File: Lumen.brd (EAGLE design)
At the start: 59.6 x 24 mm, 32 parts, among them J1 AVR_SPI_PRG_6PTH, U1 Tiny45-20-SMT, Y1 8MHZ

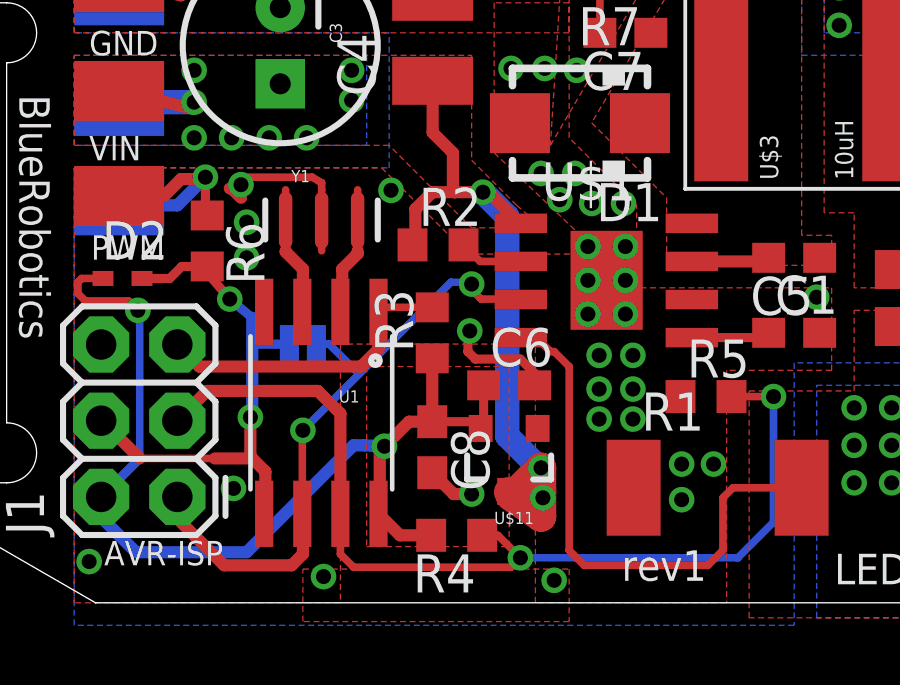
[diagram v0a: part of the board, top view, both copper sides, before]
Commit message: Fixed two minor issues in the layout with ground per J.N. suggestion. Ordering a prototype tomorrow.
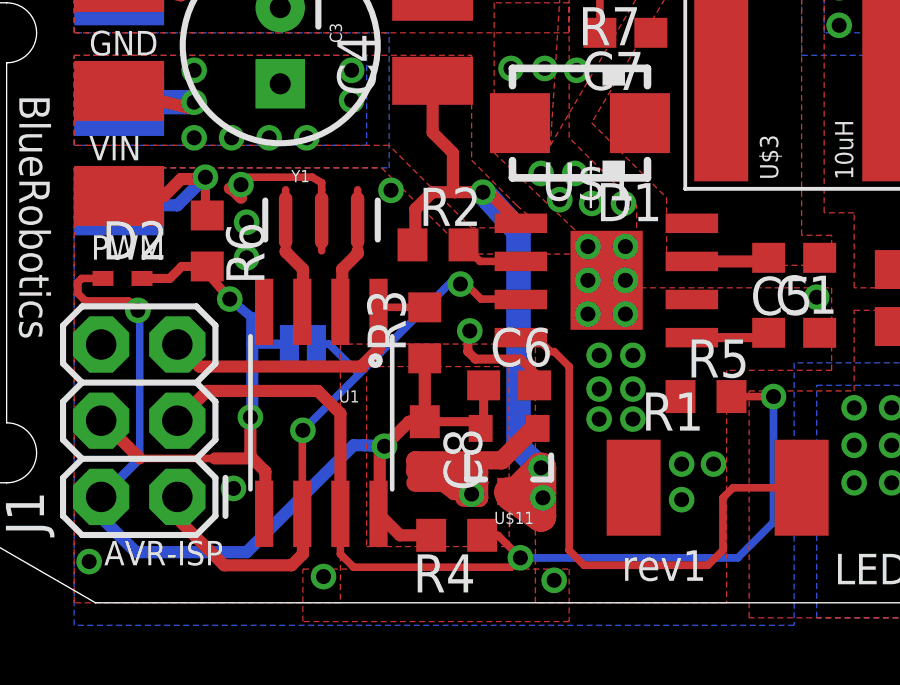
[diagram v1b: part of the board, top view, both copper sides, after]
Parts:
- moved C8 0.25 mm to (13.9, 5.19)
- moved R3 0.25 mm to (13.9, 9.00)
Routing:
- net GND: track 15.1 -> 25.9 mm
- net LED-PWM: track 21.7 -> 22.3 mm
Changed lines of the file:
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@@
 <element name="R1" library="resistor" package="R2512" value="0.082 1W" x="23.7" y="3.835"/>
 <element name="R2" library="resistor" package="R0603" value="140K" x="14.38" y="11.93"/>
-<element name="R3" library="resistor" package="R0603" value="10K" x="14.1875" y="9" rot="R90"/>
+<element name="R3" library="resistor" package="R0603" value="10K" x="13.9375" y="9" rot="R90"/>
 <element name="R4" library="resistor" package="R0603" value="3.3K 1%" x="15" y="2.25" rot="R180"/>
 <element name="R5" library="resistor" package="R0603" value="10K NTC" x="23.3125" y="6.875"/>
@@
 <attribute name="PROD_ID" value="IC-08922" x="10.49" y="6.32" size="1.778" layer="27" rot="R180" display="off"/>
 </element>
-<element name="C8" library="resistor" package="C0603" value="0.1uF" x="14.1875" y="5.1875" rot="R270"/>
+<element name="C8" library="resistor" package="C0603" value="0.1uF" x="13.9375" y="5.1875" rot="R270"/>
 <element name="Y1" library="SparkFun-FreqCtrl" package="RESONATOR-SMD" value="8MHZ" x="10.5" y="12.75">
 <attribute name="PROD_ID" value="XTAL-08900" x="10.5" y="12.75" size="1.778" layer="27" display="off"/>
@@
 <via x="18.4375" y="13.4375" extent="1-16" drill="0.5"/>
 <wire x1="15.5" y1="3.625" x2="14.9" y2="3.625" width="0.4064" layer="1"/>
-<wire x1="14.9" y1="3.625" x2="14.1875" y2="4.3375" width="0.4064" layer="1"/>
+<wire x1="14.9" y1="3.625" x2="13.9375" y2="4.3375" width="0.4064" layer="1"/>
 <polygon width="0.4064" layer="1" isolate="0.254" thermals="no">
 <vertex x="2.25" y="14.5"/>
@@
 <via x="19.75" y="7.125" extent="1-16" drill="0.5"/>
 <via x="19.75" y="6.125" extent="1-16" drill="0.5"/>
+<wire x1="17.75" y1="5.875" x2="17.625" y2="5.875" width="0.6096" layer="1"/>
+<wire x1="17.625" y1="5.875" x2="16.5" y2="4.75" width="0.6096" layer="1"/>
+<wire x1="16.5" y1="4.75" x2="13.625" y2="4.75" width="0.6096" layer="1"/>
+<wire x1="13.625" y1="4.75" x2="13.625" y2="4.375" width="0.6096" layer="1"/>
+<wire x1="13.625" y1="4.375" x2="15.75" y2="4.375" width="0.6096" layer="1"/>
+<wire x1="15.75" y1="4.375" x2="15.75" y2="4" width="0.6096" layer="1"/>
+<wire x1="13.625" y1="4" x2="15.75" y2="4" width="0.6096" layer="1"/>
+<wire x1="15.75" y1="4" x2="15.75" y2="3.5" width="0.6096" layer="1"/>
+<wire x1="15.75" y1="3.5" x2="15.25" y2="3.5" width="0.6096" layer="1"/>
 </signal>
 <signal name="N$1">
@@
 <via x="17.8125" y="4.5" extent="1-16" drill="0.5"/>
 <wire x1="17.8125" y1="4.5" x2="17.75" y2="4.5" width="0.3048" layer="16"/>
-<wire x1="17.75" y1="4.5" x2="16.6875" y2="5.5625" width="0.8128" layer="16"/>
-<wire x1="16.6875" y1="5.5625" x2="16.6875" y2="12.875" width="0.8128" layer="16"/>
-<wire x1="16.6875" y1="12.875" x2="15.875" y2="13.6875" width="0.8128" layer="16"/>
+<wire x1="17.75" y1="4.5" x2="17.0625" y2="5.1875" width="0.8128" layer="16"/>
+<wire x1="17.0625" y1="5.1875" x2="17.0625" y2="12.375" width="0.8128" layer="16"/>
+<wire x1="17.0625" y1="12.375" x2="15.875" y2="13.6875" width="0.8128" layer="16"/>
 <via x="15.875" y="13.6875" extent="1-16" drill="0.5"/>
 <wire x1="15.875" y1="13.6875" x2="16.1025" y2="13.6875" width="0.3048" layer="1"/>
@@
 <wire x1="9.855" y1="5.8325" x2="9.875" y2="5.75" width="0.254" layer="1"/>
 <via x="9.875" y="5.75" extent="1-16" drill="0.5"/>
-<wire x1="15.4375" y1="10.6875" x2="15.5" y2="10.625" width="0.254" layer="16"/>
-<via x="15.5" y="10.625" extent="1-16" drill="0.5"/>
-<wire x1="15.5" y1="10.625" x2="15.5" y2="10.4375" width="0.254" layer="1"/>
-<wire x1="15.5" y1="10.4375" x2="15.8125" y2="10.125" width="0.254" layer="1"/>
+<wire x1="15.4375" y1="10.6875" x2="15.125" y2="10.625" width="0.254" layer="16"/>
+<via x="15.125" y="10.625" extent="1-16" drill="0.5"/>
+<wire x1="15.125" y1="10.625" x2="15.25" y2="10.6875" width="0.254" layer="1"/>
+<wire x1="15.25" y1="10.6875" x2="15.8125" y2="10.125" width="0.254" layer="1"/>
 <wire x1="15.8125" y1="10.125" x2="17.125" y2="10.125" width="0.254" layer="1"/>
 <wire x1="17.125" y1="10.125" x2="17.14" y2="10.11" width="0.254" layer="1"/>
@@
 <contactref element="R4" pad="2"/>
 <contactref element="C8" pad="1"/>
-<wire x1="14.1875" y1="6.0375" x2="14.1875" y2="8.15" width="0.4064" layer="1"/>
+<wire x1="13.9375" y1="6.0375" x2="13.9375" y2="8.15" width="0.4064" layer="1"/>
 <wire x1="14.15" y1="2.25" x2="13.1122" y2="2.25" width="0.4064" layer="1"/>
 <wire x1="13.1122" y1="2.25" x2="12.395" y2="2.9672" width="0.4064" layer="1"/>
-<wire x1="14.1875" y1="6.0375" x2="13.4125" y2="6.0375" width="0.4064" layer="1"/>
+<wire x1="13.9375" y1="6.0375" x2="13.4125" y2="6.0375" width="0.4064" layer="1"/>
 <wire x1="12.59375" y1="5.21875" x2="12.4375" y2="5.0625" width="0.4064" layer="1"/>
 <wire x1="12.4375" y1="5.0625" x2="12.4375" y2="3.0097" width="0.4064" layer="1"/>
@@
 <wire x1="4.3125" y1="1.6875" x2="8" y2="1.6875" width="0.4064" layer="16"/>
 <contactref element="U$11" pad="2"/>
-<wire x1="14.1875" y1="6.0375" x2="15.7625" y2="6.0375" width="0.3048" layer="1"/>
+<wire x1="13.9375" y1="6.0375" x2="15.7625" y2="6.0375" width="0.3048" layer="1"/>
 <wire x1="15.7625" y1="6.0375" x2="15.8" y2="5.8125" width="0.3048" layer="1"/>
 <contactref element="C6" pad="1"/>
@@
 <contactref element="U1" pad="1"/>
 <contactref element="R3" pad="2"/>
-<wire x1="14.1875" y1="9.85" x2="12.5468" y2="9.85" width="0.254" layer="1"/>
+<wire x1="13.9375" y1="9.85" x2="12.5468" y2="9.85" width="0.254" layer="1"/>
 <wire x1="12.5468" y1="9.85" x2="12.395" y2="9.6982" width="0.254" layer="1"/>
 <wire x1="12.395" y1="9.6982" x2="12.395" y2="8.4575" width="0.4064" layer="1"/>

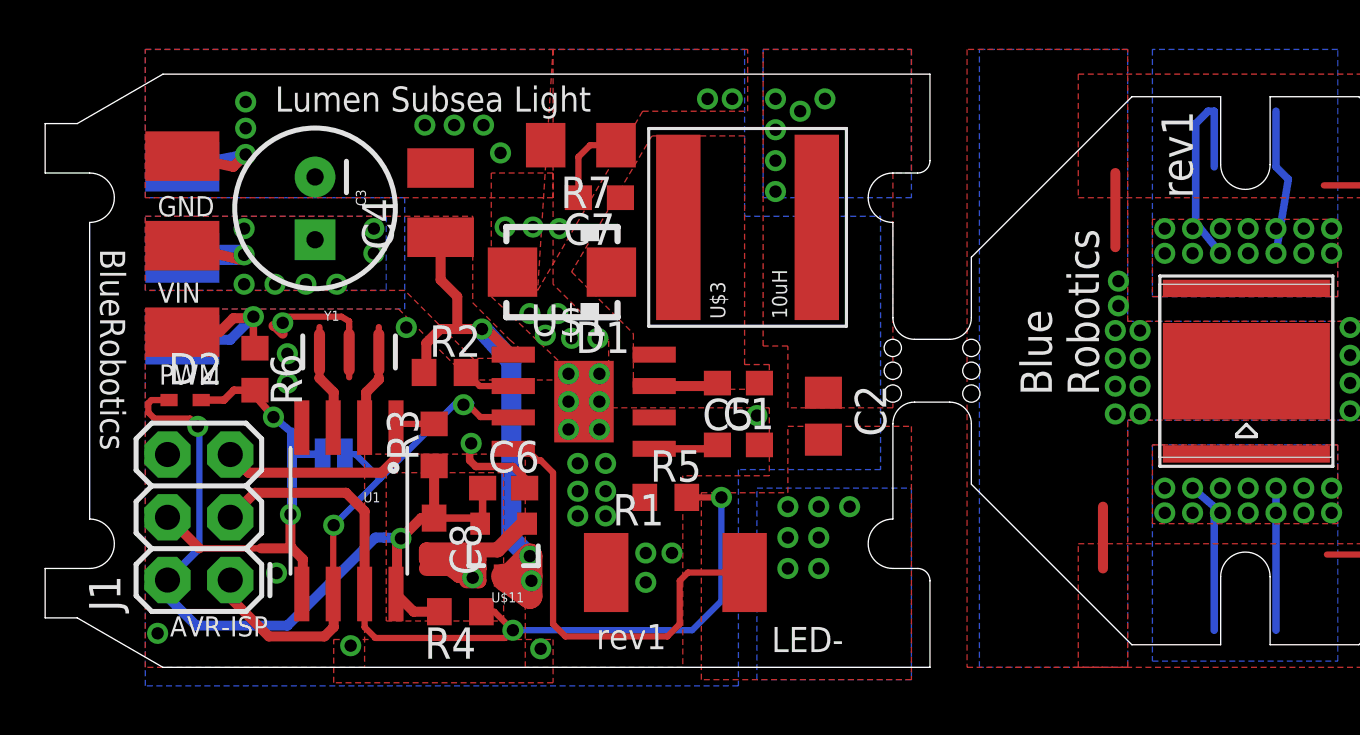
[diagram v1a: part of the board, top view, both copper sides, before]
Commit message: Adjusted signal pull-down for 3.3V compatibility.
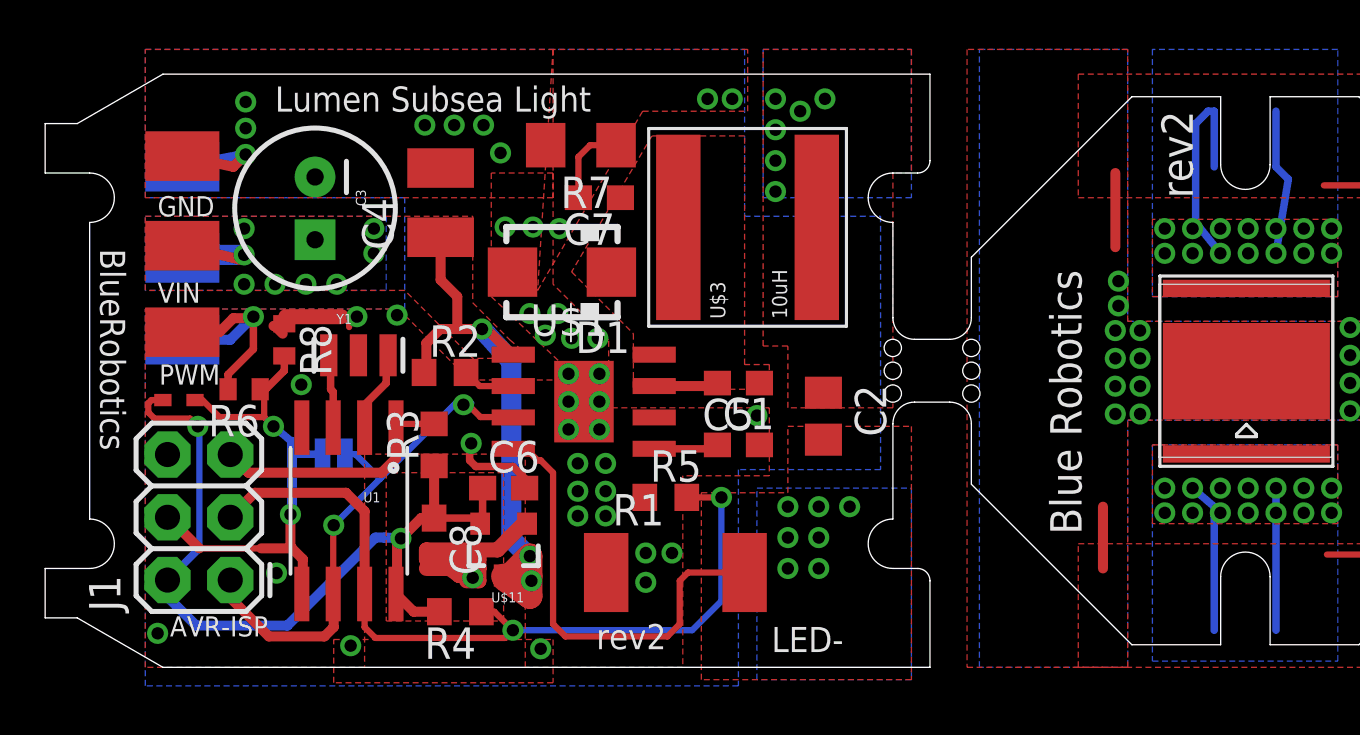
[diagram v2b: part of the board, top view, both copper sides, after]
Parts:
- added R8: 300K, resistor:R0402
- R6: value 27K -> 15K 1/5W; device resistor:R0603 -> resistor:R0402
- U$10: value LOGOBR-LOGO-MS -> LOGOBR-LOGO-MS-COPPER; device BlueRobotics-Main:BR-LOGO-MEDIUM-SMALL -> BlueRobotics-Main:BR-LOGO-MEDIUM-SMALL-COPPER
- Y1: value 8MHZ -> 8Mhz; device SparkFun-FreqCtrl:RESONATOR-SMD -> SparkFun:RESONATOR-SMD
- moved U$10 18.3 mm to (24.6, 12.8), flipped to the bottom
- moved R6 0.92 mm to (6.25, 11.2), turned to 180 degrees
- moved Y1 0.40 mm to (10.9, 12.6)
- moved D2 0.25 mm to (3.56, 10.8)
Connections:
- net GND: now also R8.1
- net SIGNAL: now also R6.1, R8.2; no longer R6.2
- net SIGNAL_HV: now also R6.2; no longer R6.1
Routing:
- net SIGNAL: track 18.3 -> 21.1 mm
- net SIGNAL_HV: track 7.70 -> 9.76 mm
- net N$7: track 2.27 -> 3.32 mm
- net N$6: track 2.28 -> 3.00 mm
- net GND: vias 43 -> 42
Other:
- board text added: "Daisy chain pads"
- board text added: "rev2"
- board text removed: "rev1"

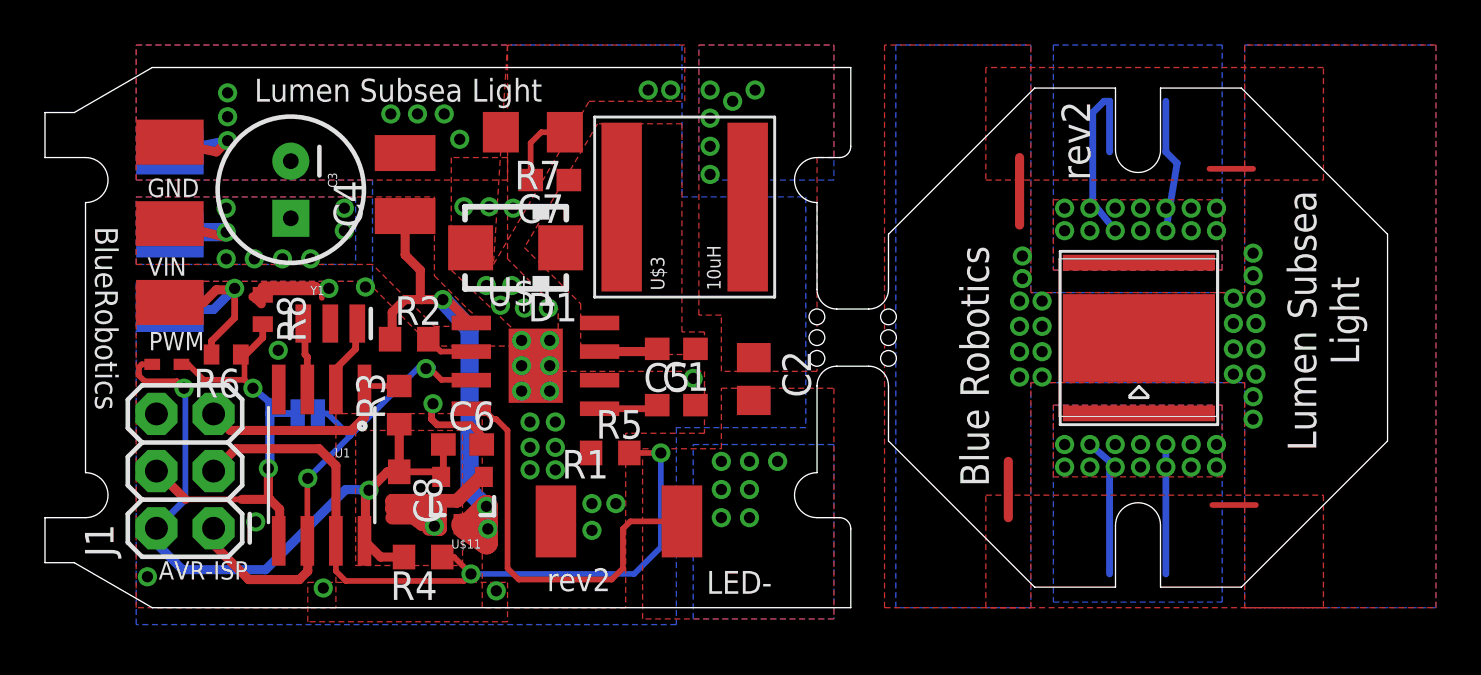
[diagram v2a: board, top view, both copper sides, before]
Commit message: Rearranged boards for manufacturability. Changed 0402 footprint.
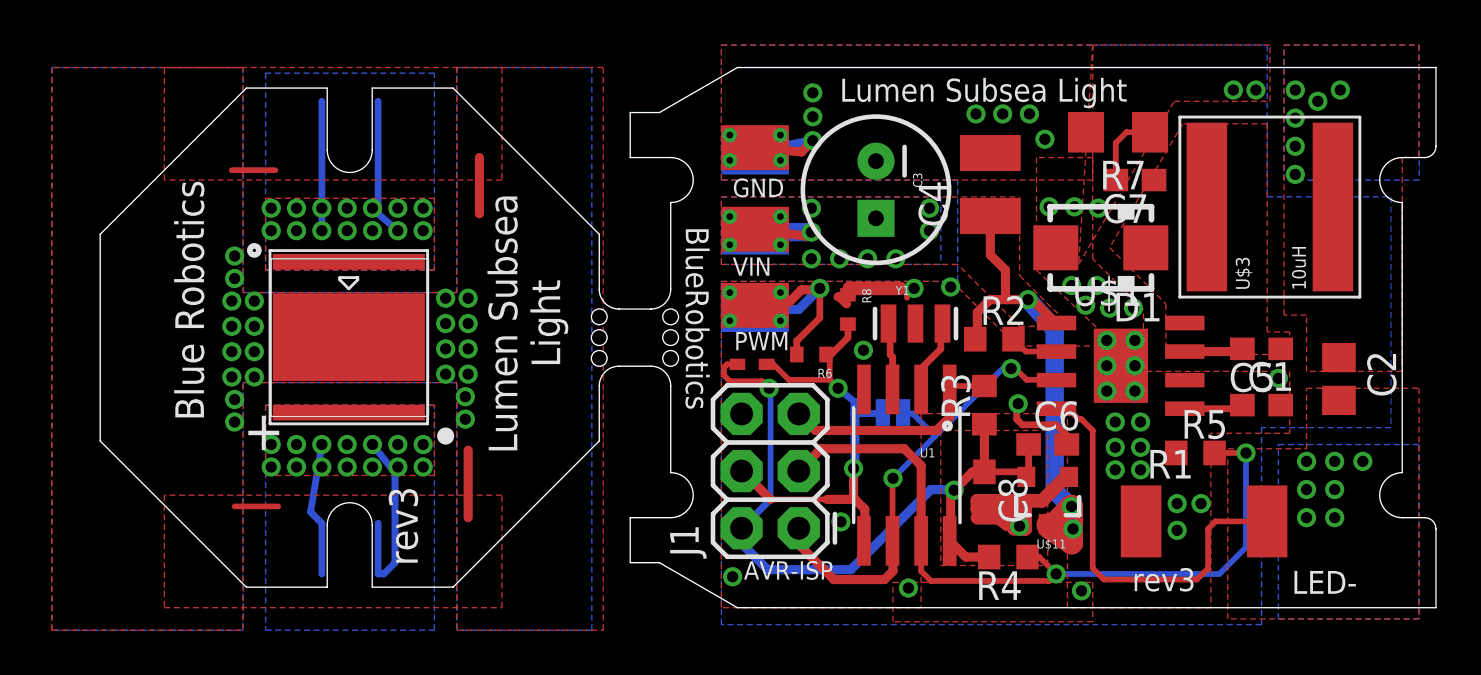
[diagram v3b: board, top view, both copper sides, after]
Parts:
- R6, R8: device resistor:R0402 -> BlueRobotics-Main:C0402
- moved U$2 35.7 mm to (11.7, 15.4), turned to 270 degrees
- moved U$8 26.0 mm to (29.8, 16.8)
- moved U$9 26.0 mm to (29.8, 20.4)
- moved U$5 26.0 mm to (29.8, 16.7)
- moved U$7 26.0 mm to (29.8, 13.4)
- moved C4 26.0 mm to (40.2, 18.8)
- moved R1 26.0 mm to (49.7, 3.83)
- moved C1 26.0 mm to (52.2, 9.00)
- moved C3 26.0 mm to (35.1, 18.6)
- moved C5 26.0 mm to (52.2, 11.5)
- moved C6 26.0 mm to (42.8, 7.25)
- moved C7 26.0 mm to (46.6, 19.0)
- moved C8 26.0 mm to (39.9, 5.19)
- moved D1 26.0 mm to (45.1, 16.0)
- moved D2 26.0 mm to (29.6, 10.8)
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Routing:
- net SIGNAL_HV: track 9.76 -> 15.8 mm, vias 1 -> 5
- net VIN: track 32.7 -> 32.6 mm, vias 11 -> 15
- net GND: vias 42 -> 46
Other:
- board size 59.6 x 24 mm -> 59.3 x 24 mm
- board text added: "+"
- board text added: "rev3"
- board text removed: "Anode"
- board text removed: "rev2"

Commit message: Minor update to rev4 with larger solder holes for capacitor and silkscreen changes.
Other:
- board text added: "rev4"
- board text removed: "rev3"
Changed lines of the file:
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@@
 <vertex x="14.75" y="4"/>
 </polygon>
-<text x="19.5" y="12.625" size="1.27" layer="21" font="vector" rot="R270" align="center">Lumen Subsea
+<text x="4.125" y="11.25" size="1.27" layer="21" font="vector" rot="SR270" align="center">Lumen Subsea
 Light</text>
-<text x="14.125" y="3.625" size="1.27" layer="21" font="vector" rot="R270" align="center">rev3</text>
-<text x="4.625" y="19" size="1.27" layer="21" font="vector" rot="R270" align="center-left">Blue Robotics</text>
+<text x="14.125" y="3.625" size="1.27" layer="21" font="vector" rot="R270" align="center">rev4</text>
+<text x="18.75" y="18.75" size="1.27" layer="21" font="vector" rot="SR270" align="center-left">Blue Robotics</text>
 <polygon width="0.254" layer="29">
 <vertex x="59.3125" y="23.75"/>
@@
 <text x="56" y="22.5" size="1.016" layer="22" rot="MR270" align="center-left">LED+</text>
 <text x="33.5" y="23.5" size="1.016" layer="21" align="top-left">Lumen Subsea Light</text>
-<text x="46.5" y="1.75" size="1.016" layer="21" align="top-left">rev3</text>
+<text x="46.5" y="1.75" size="1.016" layer="21" align="top-left">rev4</text>
 <text x="27.6875" y="16.9375" size="1.016" layer="21" rot="SR270" align="top-left">BlueRobotics</text>
 <text x="7.375" y="18.5" size="1.016" layer="22" rot="MR180" align="top-left">LED-</text>
@@
 <circle x="7.5" y="15.875" radius="0.125" width="0.4064" layer="21"/>
 <circle x="16" y="7.625" radius="0.176775" width="0.4064" layer="21"/>
+<polygon width="0.254" layer="29">
+<vertex x="57.25" y="23.75"/>
+<vertex x="55.375" y="23.75"/>
+<vertex x="55.375" y="22.375"/>
+<vertex x="57.25" y="22.375"/>
+</polygon>
 </plain>
 <attributes>
@@
 <via x="53.75" y="23" extent="1-16" drill="0.5"/>
 <via x="54.75" y="22.5" extent="1-16" drill="0.5"/>
-<via x="55.75" y="23" extent="1-16" drill="0.5"/>
 <via x="53.75" y="21.75" extent="1-16" drill="0.5"/>
 <via x="53.75" y="20.5" extent="1-16" drill="0.5"/>
@@
 <wire x1="31.25" y1="10.125" x2="33.0625" y2="10.125" width="0.254" layer="1"/>
 <wire x1="33.0625" y1="10.125" x2="33.4375" y2="9.75" width="0.254" layer="1"/>
-<wire x1="33.0625" y1="10.125" x2="33.0625" y2="11.3375" width="0.254" layer="1"/>
-<wire x1="33.0625" y1="11.3375" x2="32.9" y2="11.25" width="0.254" layer="1"/>
-<wire x1="32.9" y1="11.25" x2="33.125" y2="11.25" width="0.3048" layer="1"/>
+<wire x1="32.75" y1="11.25" x2="33.125" y2="11.25" width="0.3048" layer="1"/>
 <wire x1="33.125" y1="11.25" x2="33.875" y2="12" width="0.3048" layer="1"/>
-<wire x1="33.875" y1="12" x2="33.875" y2="12.6" width="0.3048" layer="1"/>
+<wire x1="33.875" y1="12" x2="33.875" y2="12.75" width="0.3048" layer="1"/>
+<wire x1="33.0625" y1="10.125" x2="33.0625" y2="10.3125" width="0.254" layer="1"/>
+<wire x1="33.0625" y1="10.3125" x2="32.75" y2="10.625" width="0.254" layer="1"/>
+<wire x1="32.75" y1="10.625" x2="32.75" y2="11.25" width="0.254" layer="1"/>
 </signal>
 <signal name="VCC">
@@
 <wire x1="32.5625" y1="14.125" x2="32.625" y2="14.1875" width="0.3048" layer="1"/>
 <contactref element="R6" pad="2"/>
-<wire x1="31.6" y1="11.25" x2="31.6" y2="11.85" width="0.3048" layer="1"/>
-<wire x1="31.6" y1="11.85" x2="32.625" y2="12.875" width="0.3048" layer="1"/>
-<wire x1="32.625" y1="12.875" x2="32.625" y2="14.1875" width="0.3048" layer="1"/>
+<wire x1="32.625" y1="12.75" x2="32.625" y2="14.1875" width="0.3048" layer="1"/>
 <via x="30.875" y="14" extent="1-16" drill="0.3"/>
 <wire x1="31.25" y1="13.5625" x2="30.875" y2="13.5625" width="0.4064" layer="1"/>
@@
 <wire x1="29.75" y1="13.4375" x2="30" y2="13.4375" width="0.4064" layer="1"/>
 <wire x1="30" y1="13.4375" x2="30" y2="14" width="0.4064" layer="1"/>
+<wire x1="32.625" y1="12.75" x2="31.75" y2="11.875" width="0.3048" layer="1"/>
+<wire x1="31.75" y1="11.875" x2="31.75" y2="11.25" width="0.3048" layer="1"/>
 </signal>
 <signal name="N$2">
